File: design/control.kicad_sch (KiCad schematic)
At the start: 11 parts, among them J1 Conn_01x03_Pin, U1 STM32F303RETx

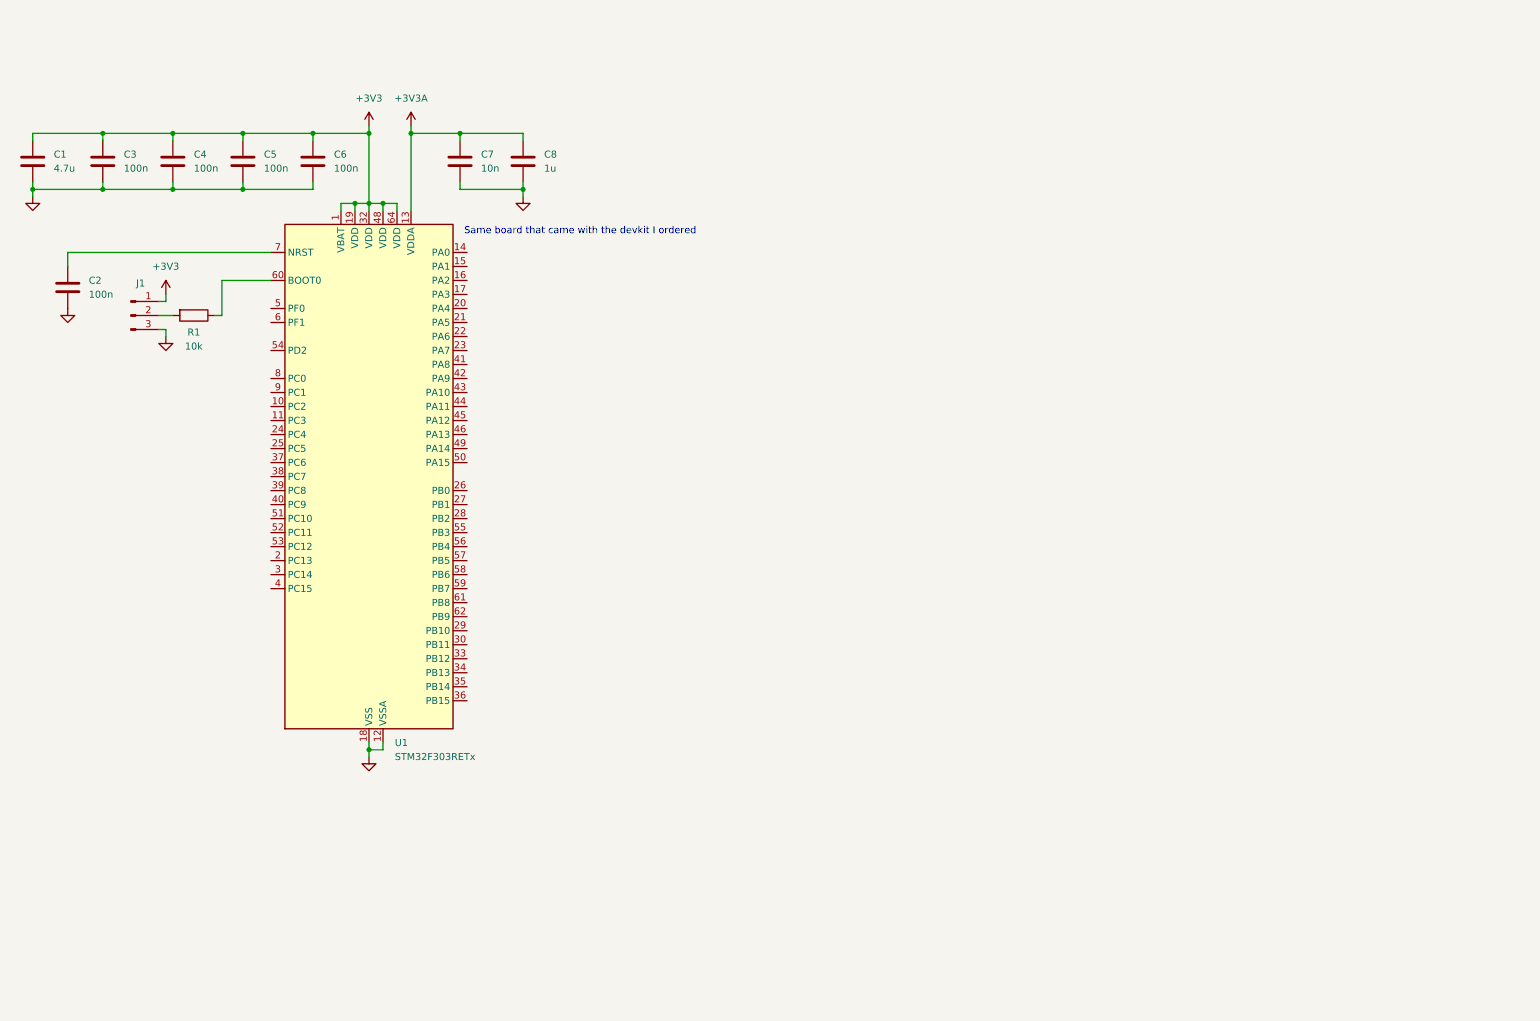
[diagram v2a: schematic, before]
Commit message: added CubeMX files, worked on microcontroller schematic
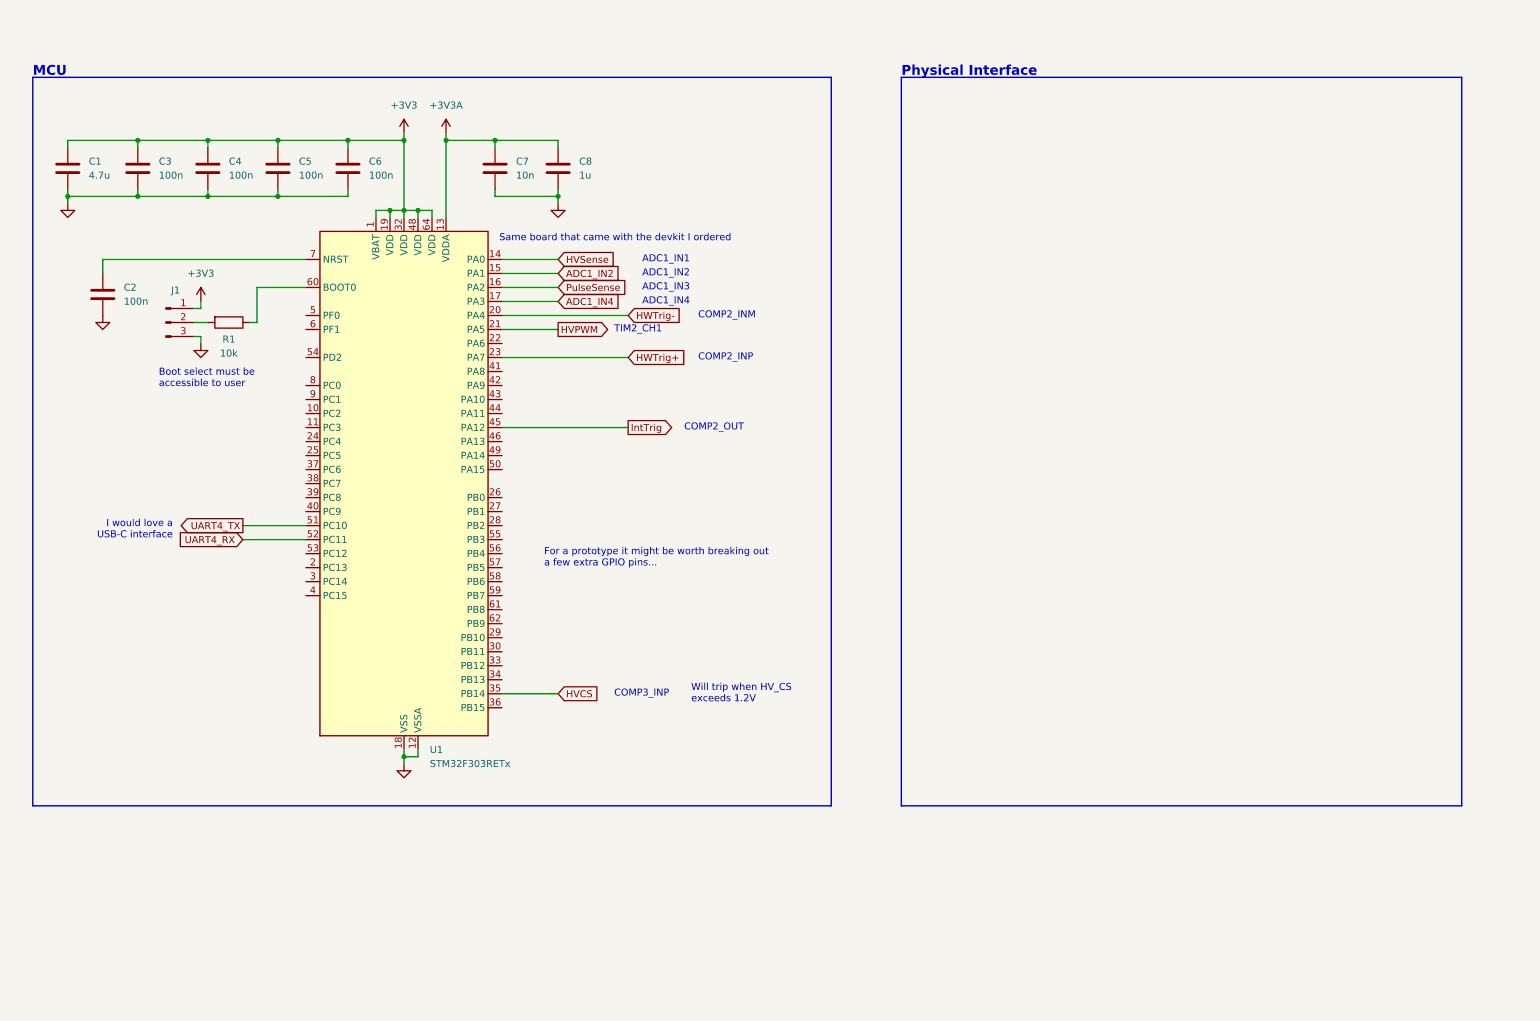
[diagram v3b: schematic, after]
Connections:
- net HVSense: now reaches U1.14 (PA0)
- net ADC1_IN2: now reaches U1.15 (PA1)
- net PulseSense: now reaches U1.16 (PA2)
- net ADC1_IN4: now reaches U1.17 (PA3)
- net HWTrig-: now reaches U1.20 (PA4)
- net HVPWM: now reaches U1.21 (PA5)
- net HWTrig+: now reaches U1.23 (PA7)
- net HVCS: now reaches U1.35 (PB14)
- net IntTrig: now reaches U1.45 (PA12)
- net UART4_TX: now reaches U1.51 (PC10)
- net UART4_RX: now reaches U1.52 (PC11)
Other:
- note added: "ADC1_IN1"
- note added: "ADC1_IN2"
- note added: "ADC1_IN3"
- note added: "ADC1_IN4"
- note added: "Boot select must be accessible to user"
- note added: "COMP2_INM"
- note added: "COMP2_INP"
- note added: "COMP2_OUT"
- note added: "COMP3_INP"
- note added: "For a prototype it might be worth breaking out a few extra GPIO pins..."
- note added: "I would love a USB-C interface"
- note added: "MCU"
- note added: "Physical Interface"
- note added: "TIM2_CH1"
- note added: "Will trip when HV_CS exceeds 1.2V"
- moved on the sheet: C1, C2, C3, C4, C5, C6, C7, C8, J1, R1, U1

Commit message: _
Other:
- note added: "It might make more sense for PulseSense to go to a comparator, since it could also stop the HV generation when the switch is closed"
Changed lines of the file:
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@@
+		)
+	)
+	(text "It might make more sense for\nPulseSense to go to a comparator, since it could also \nstop the HV generation when the switch is closed"
+		(exclude_from_sim no)
+		(at 142.494 64.516 0)
+		(effects
+			(font
+				(size 1.27 1.27)
+			)
+			(justify left)
 		)
 	)

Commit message: figuring out triggering scheme
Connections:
- net HWTrig-: no longer names the net of U1.20 (PA4)
- no-connect marks 0 -> 1
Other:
- note added: "DAC1_OUT1"
- note removed: "COMP2_INM"
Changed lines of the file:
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@@
 		)
 	)
-	(text "COMP2_INM"
-		(exclude_from_sim no)
-		(at 139.7 68.58 0)
+	(text "DAC1_OUT1"
+		(exclude_from_sim no)
+		(at 105.918 68.834 0)
 		(effects
 			(font
@@
 		(color 0 0 0 0)
 	)
+	(no_connect
+		(at 104.14 68.58)
+	)
 	(wire
 		(pts
@@
 		(pts
 			(xy 104.14 88.9) (xy 127 88.9)
-		)
-		(stroke
-			(width 0)
-			(type default)
-		)
-	)
-	(wire
-		(pts
-			(xy 104.14 68.58) (xy 127 68.58)
 		)
 		(stroke
@@
 			(effects
 				(font
-					(size 1.27 1.27)
-				)
-				(justify left)
-				(hide yes)
-			)
-		)
-	)
-	(global_label "HWTrig-"
-		(shape input)
-		(at 127 68.58 0)
-		(fields_autoplaced yes)
-		(effects
-			(font
-				(size 1.27 1.27)
-			)
-			(justify left)
-		)
-		(property "Intersheetrefs" "${INTERSHEET_REFS}"
-			(at 137.8471 68.58 0)
-			(effects
-				(font

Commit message: _
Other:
- note added: "I could also set a custom threshold for this with the DAC whichcwould probably improve resolution"
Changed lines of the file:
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@@
+		)
+	)
+	(text "I could also set a custom\nthreshold for this with the DAC \nwhichcwould probably improve resolution"
+		(exclude_from_sim no)
+		(at 138.43 147.32 0)
+		(effects
+			(font
+				(size 1.27 1.27)
+			)
+			(justify left bottom)
 		)
 	)

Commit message: _
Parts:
- added JCS1, JSENSE1: Conn-OScope, symbol Connector:Conn_Coaxial
- added JHWTRIG1: SMB, symbol Connector:Conn_Coaxial
- added JPULSE1: SMA, symbol Connector:Conn_Coaxial
- added P1: USB_C_Plug_USB2.0, symbol Connector:USB_C_Plug_USB2.0
- added U4: CP2102N-Axx-xQFN20, Package_DFN_QFN:SiliconLabs_QFN-20-1EP_3x3mm_P0.5mm, symbol Interface_USB:CP2102N-Axx-xQFN20
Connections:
- net GND: now also JCS1.2 (Ext), JHWTRIG1.2 (Ext), JSENSE1.2 (Ext)
- net HWTrig+: now also JHWTRIG1.1 (In)
- net PulseSense: now also JSENSE1.1 (In)
- net UART4_RX: now also U4.20 (~{TXT}/GPIO.2)
- net UART4_TX: now also U4.19 (~{RXT}/GPIO.3)
- new net: U4.12 (GND), U4.21 (GND), U4.3 (GND)
- new net: P1.A1 (GND), P1.A12 (GND), P1.B1 (GND), P1.B12 (GND)
- new net: P1.A4 (VBUS), P1.A9 (VBUS), P1.B4 (VBUS), P1.B9 (VBUS)
- new net GNDHV: JPULSE1.2 (Ext)
- new net PULSE+: JPULSE1.1 (In)
- new net PulseCS: JCS1.1 (In)
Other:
- note removed: "I would love a USB-C interface"

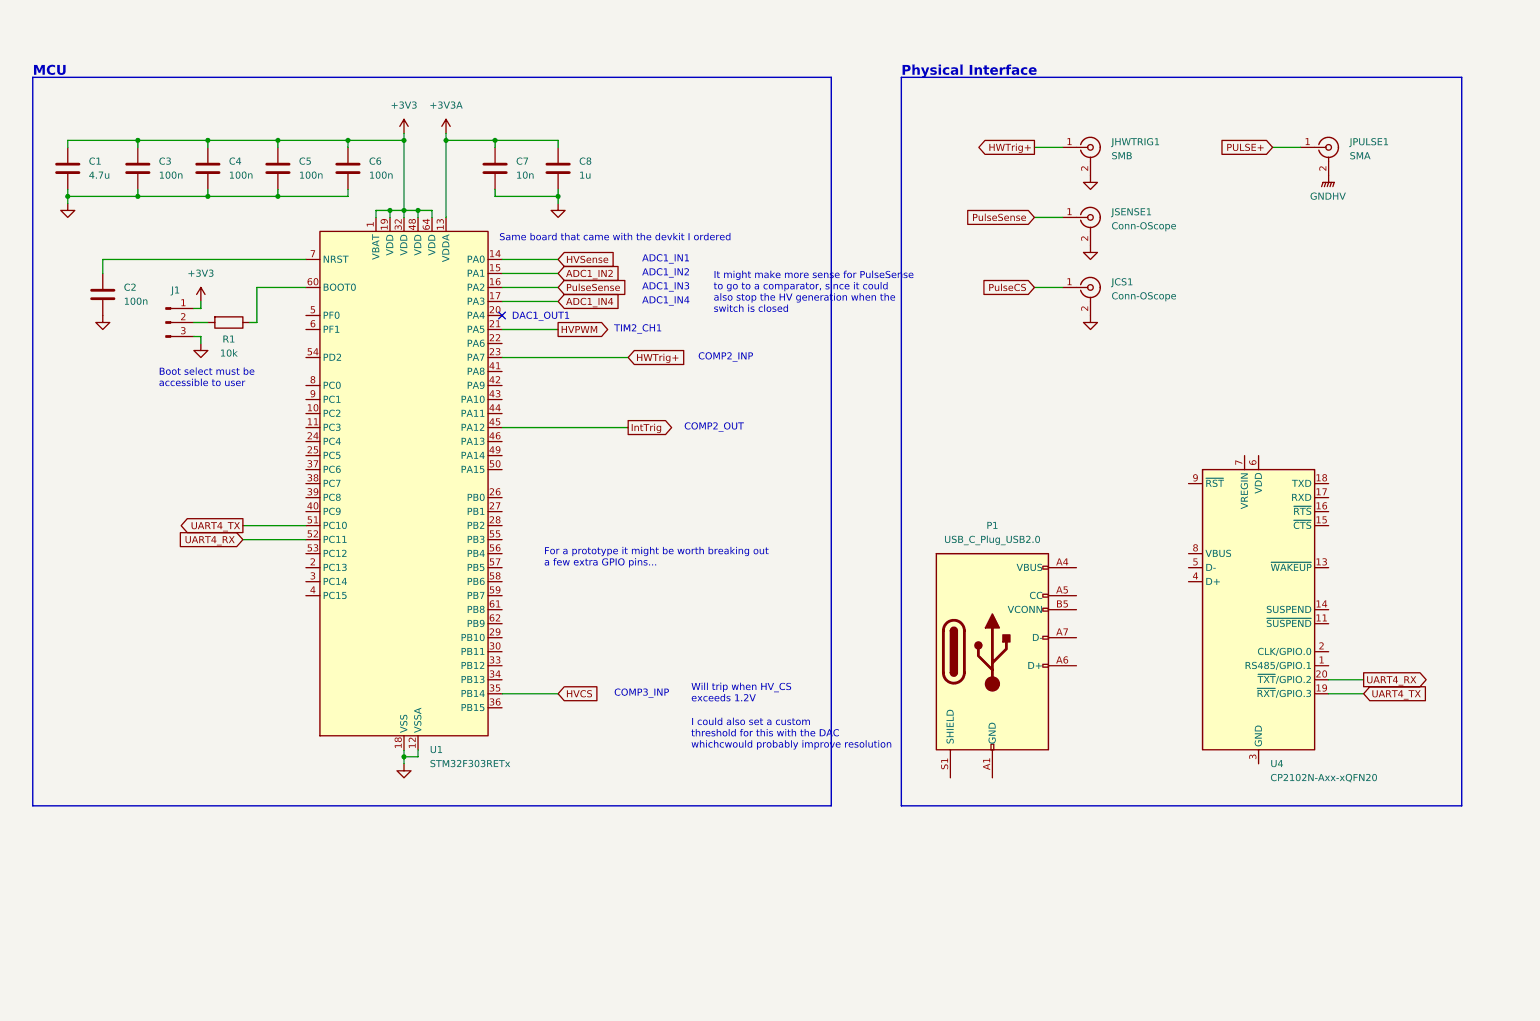
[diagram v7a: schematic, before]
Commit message: started USB-C interface design
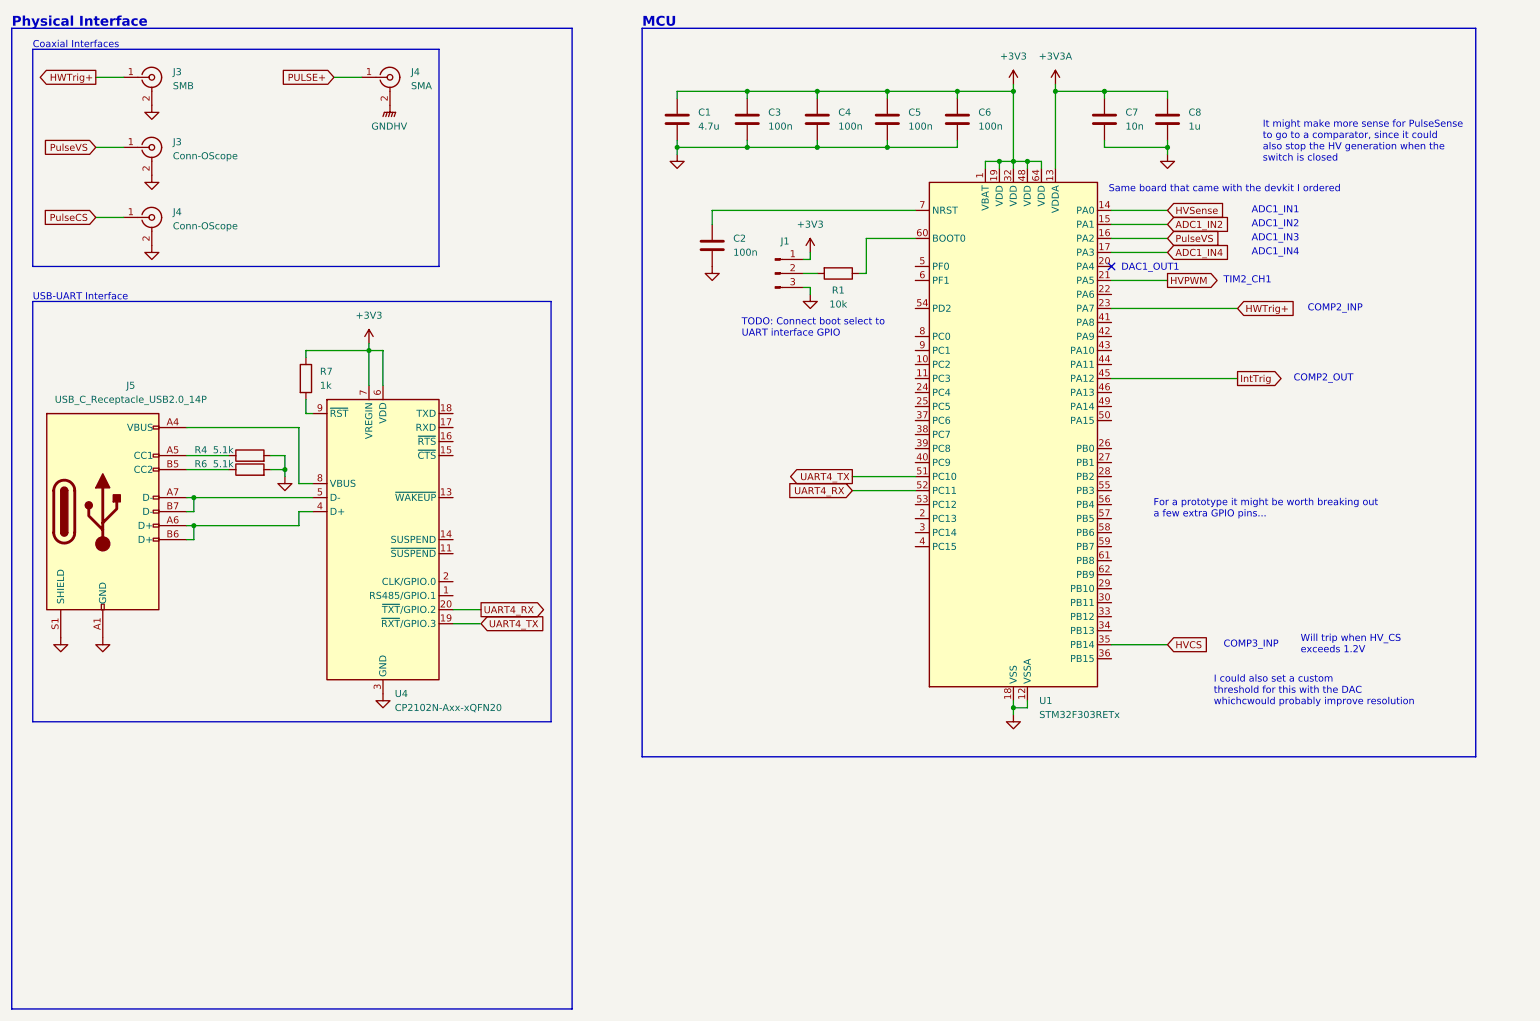
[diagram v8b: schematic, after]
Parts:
- removed JHWTRIG1: SMB, symbol Connector:Conn_Coaxial
- removed JPULSE1: SMA, symbol Connector:Conn_Coaxial
- removed P1: USB_C_Plug_USB2.0, symbol Connector:USB_C_Plug_USB2.0
- added J3: SMB, symbol Connector:Conn_Coaxial
- added J4: SMA, symbol Connector:Conn_Coaxial
- added J5: USB_C_Receptacle_USB2.0_14P, symbol Connector:USB_C_Receptacle_USB2.0_14P
- added R4, R6: 5.1k, symbol Device:R
- added R7: 1k, symbol Device:R
- renumbered JSENSE1 to J3, JCS1 to J4
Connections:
- net +3V3: now also U4.6 (VDD), U4.7 (VREGIN), R7.1
- net GND: now also U4.12 (GND), U4.21 (GND), U4.3 (GND), J3.2 (Ext), J5.A1 (GND), J5.A12 (GND), J5.B1 (GND), J5.B12 (GND), J5.S1 (SHIELD), R4.2, R6.2
- net GNDHV: now also J4.2 (Ext)
- net HWTrig+: now also J3.1 (In)
- net PULSE+: now also J4.1 (In)
- net at U4.4 (D+): now also J5.A6 (D+), J5.B6 (D+)
- net at U4.5 (D-): now also J5.A7 (D-), J5.B7 (D-)
- net at U4.8 (VBUS): now also J5.A4 (VBUS), J5.A9 (VBUS), J5.B4 (VBUS), J5.B9 (VBUS)
- net at U4.9 (~{RST}): now also R7.2
- net PulseSense renamed PulseVS
- new net: J5.A5 (CC1), R4.1
- new net: J5.B5 (CC2), R6.1
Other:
- note added: "Coaxial Interfaces"
- note added: "TODO: Connect boot select to UART interface GPIO"
- note added: "USB-UART Interface"
- note removed: "Boot select must be accessible to user"
- moved on the sheet: C1, C2, C3, C4, C5, C6, C7, C8, J1, J3, J4, R1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
